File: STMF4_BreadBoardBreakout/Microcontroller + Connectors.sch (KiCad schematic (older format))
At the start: 13 parts, among them J1 PORT A, J10 SPI1, J11 SWD, J12 PORT E, J2 USART1, J3 USB_B_Micro, J4 PORT B, J5 USART2, J6 PORT C, J7 I2C3, J8 DCMI SPI CAM, J9 PORT D, U1 STM32F446VETx

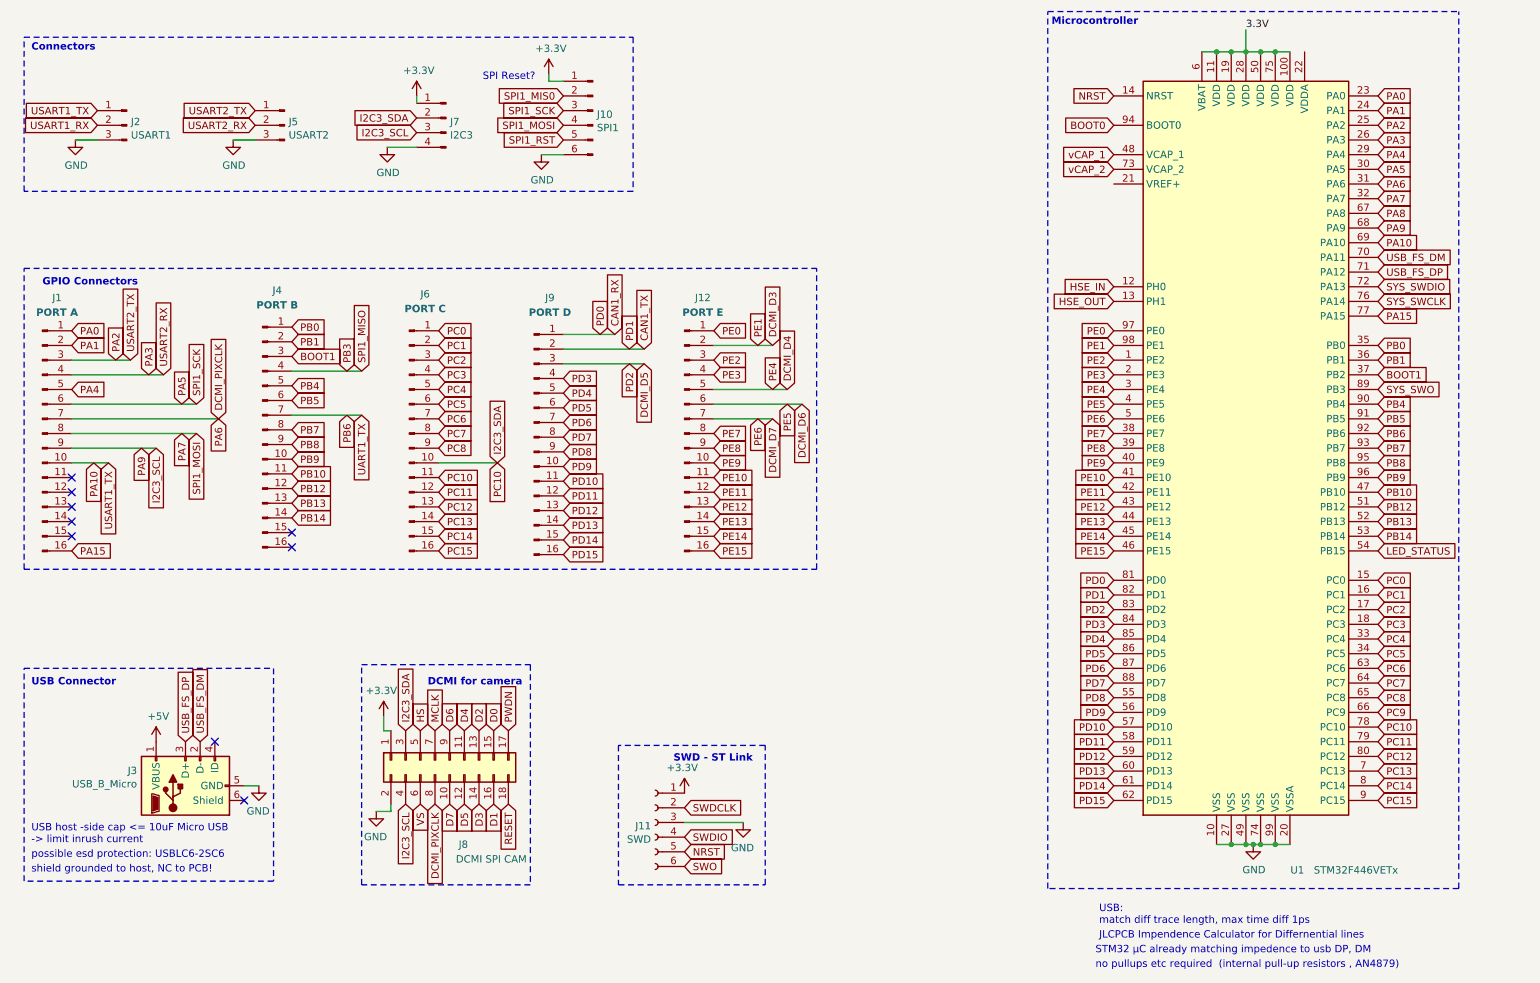
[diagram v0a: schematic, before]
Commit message: reduce size in pcb, fix second sheet, main routing finished
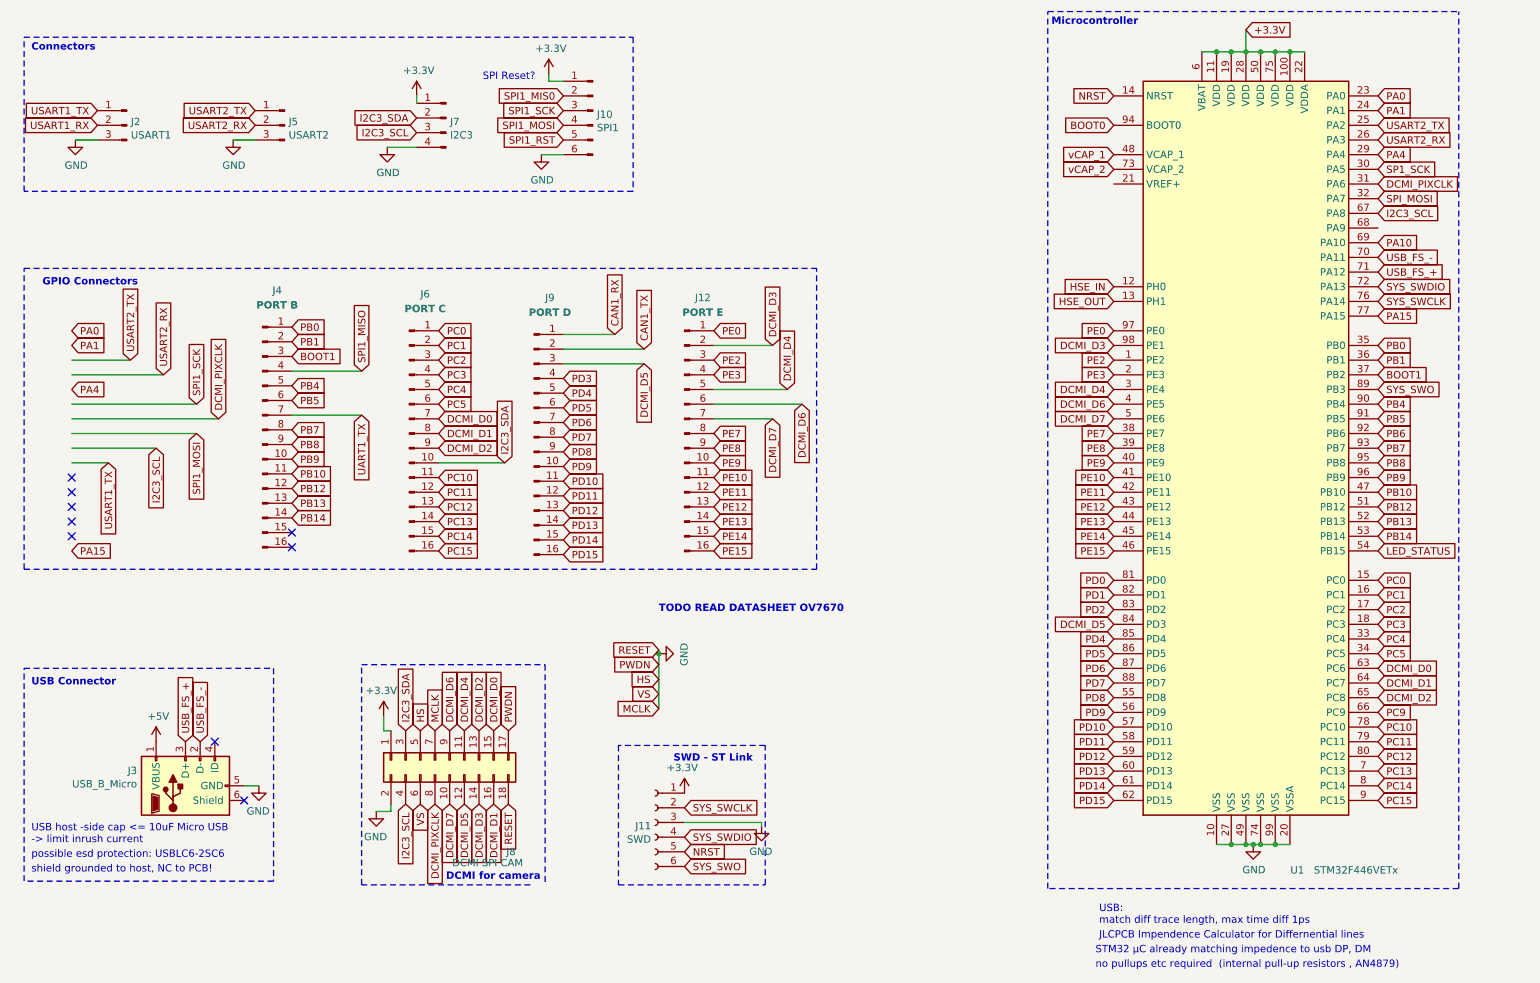
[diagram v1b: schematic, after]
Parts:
- removed J1: PORT A, Connector_PinHeader_2.54mm:PinHeader_1x16_P2.54mm_Vertical, symbol STMF4_BreadBoardBreakout-rescue:Conn_01x16_Male-Connector-STMF4_BreadBoardBreak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
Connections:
- net labels added: DCMI_D0, DCMI_D1, DCMI_D2, SP1_SCK, SPI_MOSI, USB_FS_+, USB_FS_-
- net labels removed: 3.3V, D0, D1, D2, D3, D4, D5, D6, D7, PA2, PA3, PA5, PA6, PA7, PA8, PA9, PB3, PC6, PC7, PC8, PE1, PE4, PE5, PE6, SWDCLK, SWDIO, SWO, USB_FS_DM, USB_FS_DP
- wire segments 43 -> 47
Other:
- note added: "TODO READ DATASHEET OV7670\n"
